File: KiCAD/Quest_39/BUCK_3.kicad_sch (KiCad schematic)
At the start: 33 parts, among them U20 AD626ANZ, U21 INA226, U22 LTM4611EV-PBF, U23 MCP4151-502E/SN

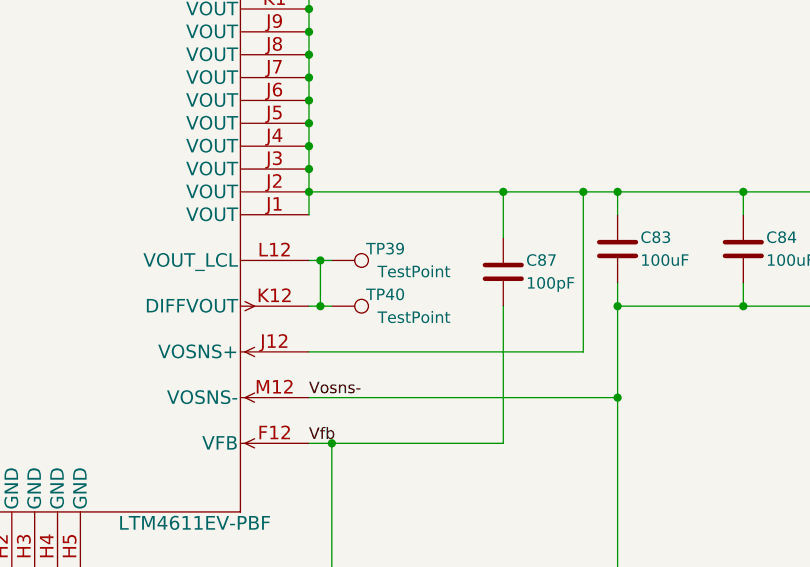
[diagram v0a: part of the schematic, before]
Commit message: Added 3rd buck converter section
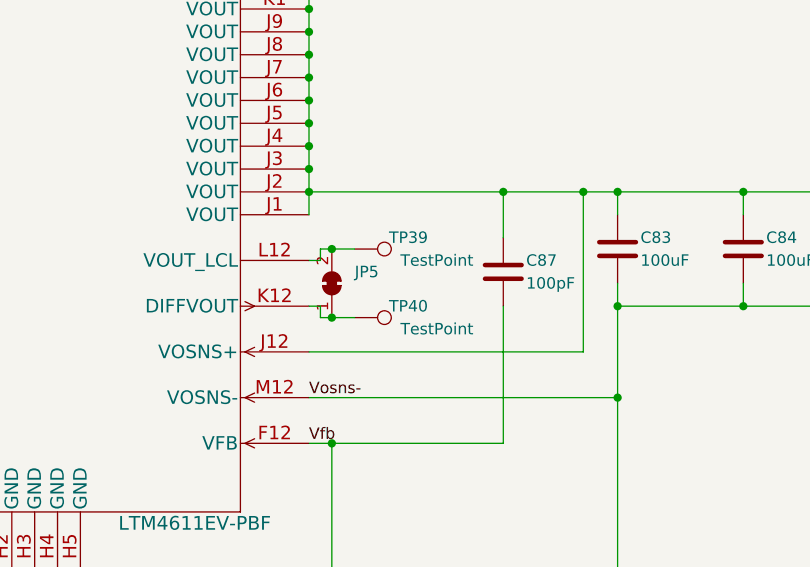
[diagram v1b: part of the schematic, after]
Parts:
- added JP5: SolderJumper_2_Bridged, Jumper:SolderJumper-2_P1.3mm_Bridged_RoundedPad1.0x1.5mm, symbol Jumper:SolderJumper_2_Bridged
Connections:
- net at TP40.1, U22.K12 (DIFFVOUT): now also JP5.1 (A); no longer TP39.1, U22.L12 (VOUT_LCL)
- new net: JP5.2 (B), TP39.1, U22.L12 (VOUT_LCL)
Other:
- moved on the sheet: TP39, TP40

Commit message: Added all the SolidWorks files, edited README
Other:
- title: (none) -> BUCK_3
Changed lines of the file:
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@@
 (kicad_sch (version 20211123) (generator eeschema)
   (paper "A3")
+  (title_block
+    (title "BUCK_3")
+    (date "2023-01-31")
+    (rev "1.0")
+  )
   (junction (at 200.66 201.93) (diameter 0) (color 0 0 0 0)
   )
